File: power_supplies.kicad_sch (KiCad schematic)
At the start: 1 part, among them J3 12V supply

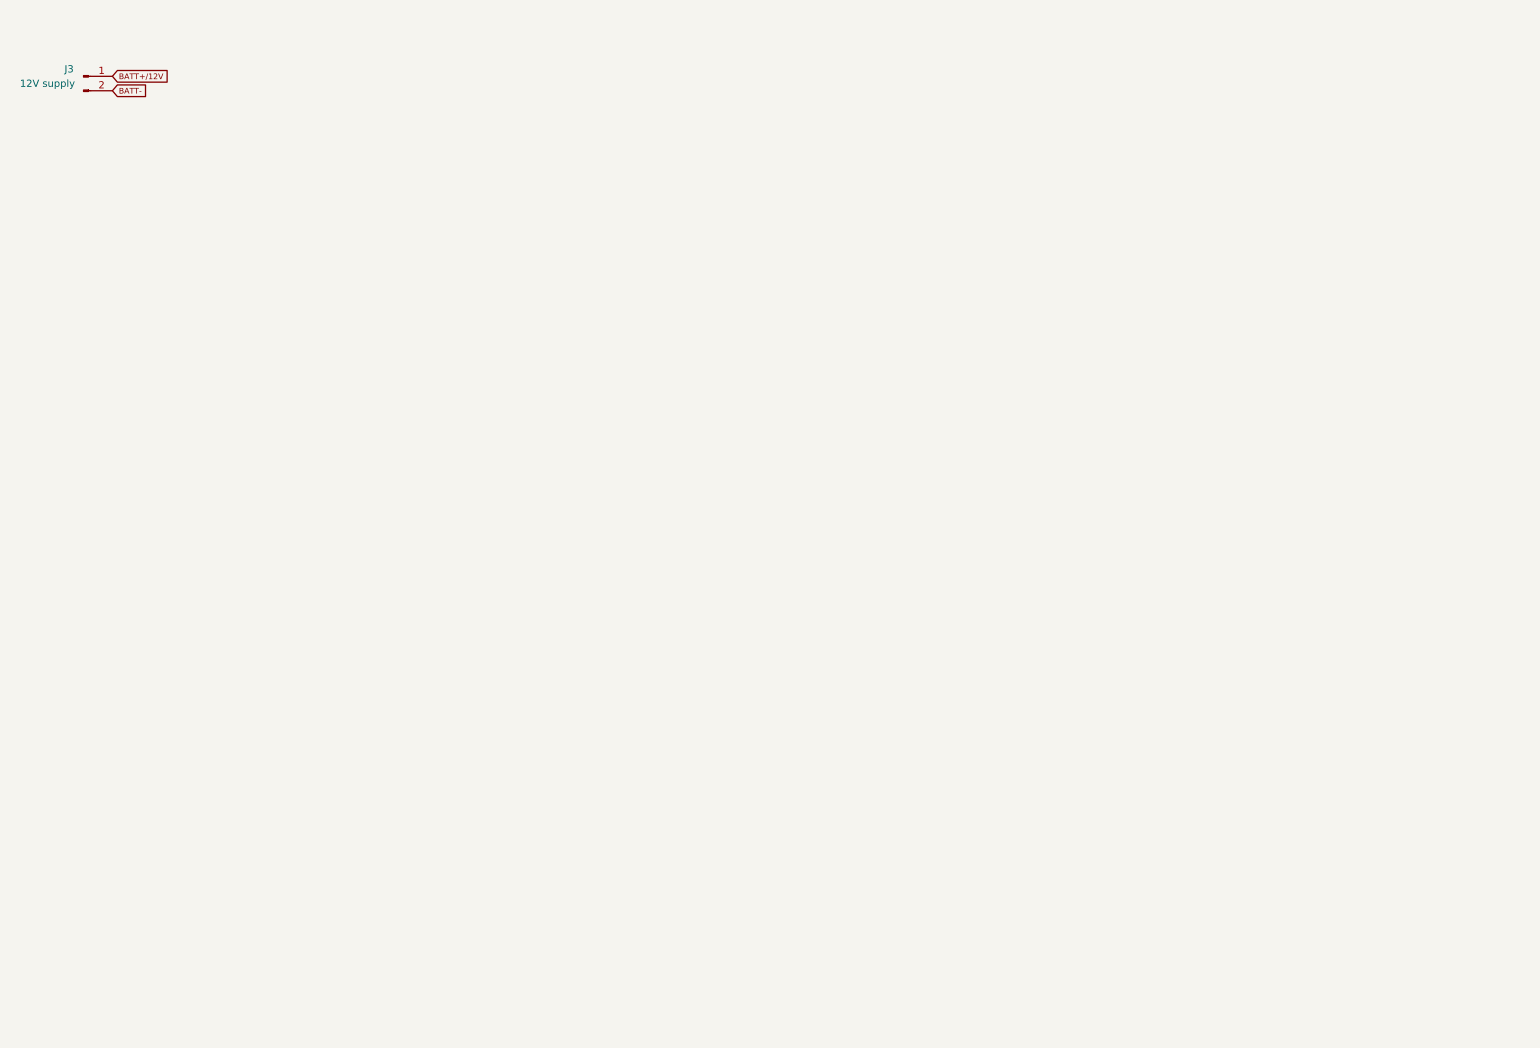
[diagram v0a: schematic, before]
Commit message: face to face switches design
with no MOVs and all other present
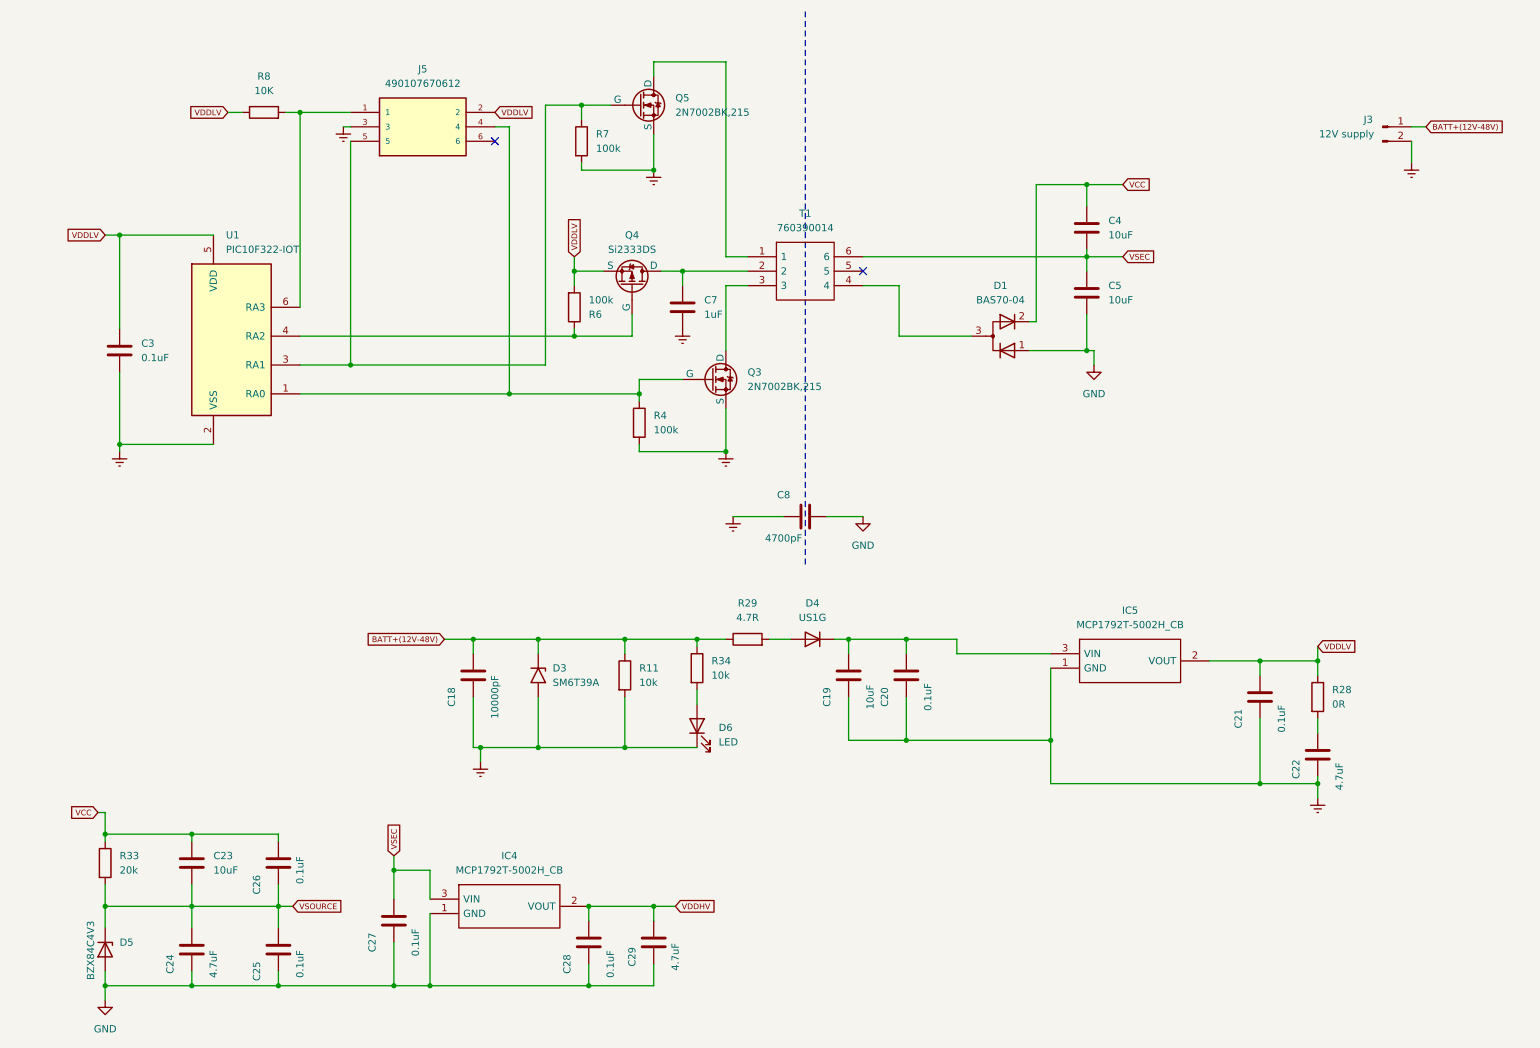
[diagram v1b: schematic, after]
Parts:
- added C18: 10000pF, Capacitor_SMD:C_0805_2012Metric, symbol Device:C
- added C19, C23: 10uF, Capacitor_SMD:C_0805_2012Metric, symbol Device:C
- added C20, C21, C25, C26, C27, C28, C3: 0.1uF, Capacitor_SMD:C_0805_2012Metric, symbol Device:C
- added C22: 4.7uF, Capacitor_SMD:C_0805_2012Metric, symbol Device:C
- added C24, C29: 4.7uF, Capacitor_SMD:C_1206_3216Metric, symbol Device:C
- added C4, C5: 10uF, Capacitor_SMD:C_1206_3216Metric, symbol Device:C
- added C7: 1uF, Capacitor_SMD:C_0805_2012Metric, symbol Device:C
- added C8: 4700pF, Capacitor_SMD:C_1812_4532Metric, symbol Device:C
- added D1: BAS70-04, Package_TO_SOT_SMD:SOT-23-3, symbol Device:D_Dual_Series_ACK_Parallel
- added D3: SM6T39A, Diode_SMD:D_SMB, symbol Diode:SM6T39A
- added D4: US1G, Diode_SMD:D_SMA, symbol Diode:US1G
- added D5: BZX84C4V3, Package_TO_SOT_SMD:SOT-23, symbol Device:D_Zener
- added D6: LED, LED_SMD:LED_0805_2012Metric, symbol Device:LED
- added IC4, IC5: MCP1792T-5002H_CB, MCP1792T-5002H_CB:SOT95P255X145-3N, symbol MCP1792T-5002H_CB:MCP1792T-5002H_CB
- added J5: 490107670612, 490107670612:WURTH_490107670612, symbol 490107670612:490107670612
- added Q3, Q5: 2N7002BK,215, Package_TO_SOT_SMD:SOT-23, symbol Simulation_SPICE:NMOS
- added Q4: Si2333DS, Package_TO_SOT_SMD:SOT-23-3, symbol Simulation_SPICE:PMOS
- added R11, R34: 10k, Resistor_SMD:R_0805_2012Metric, symbol Device:R
- added R28: 0R, Resistor_SMD:R_0805_2012Metric, symbol Device:R
- added R29: 4.7R, Resistor_SMD:R_0805_2012Metric, symbol Device:R
- added R33: 20k, Resistor_SMD:R_0805_2012Metric, symbol Device:R
- added R4, R6, R7: 100k, Resistor_SMD:R_0805_2012Metric, symbol Device:R
- added R8: 10K, Resistor_SMD:R_0805_2012Metric, symbol Device:R
- added T1: 760390014, push pull Transformer:760390015, symbol 760390014:760390014
- added U1: PIC10F322-IOT, Package_TO_SOT_SMD:SOT-23-6, symbol MCU_Microchip_PIC10:PIC10F322-IOT
- J3: footprint (none) -> TerminalBlock_Phoenix:TerminalBlock_Phoenix_MKDS-1,5-2_1x02_P5.00mm_Horizontal
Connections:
- net BATT+/12V renamed BATT+(12V-48V)
- net BATT+(12V-48V): now also C18.2, D3.1 (A1), R11.1, R29.1, R34.1
- net BATT- renamed Earth
- net Earth: now also C18.1, C19.1, C20.1, C21.1, C22.1, C3.2, C7.2, C8.1, D3.2 (A2), D6.1 (K), IC5.1 (GND), J5.3, Q3.2 (S), Q5.2 (S), R11.2, R4.2, R7.2, U1.2 (VSS)
- new net: J5.4, Q3.1 (G), R4.1, U1.1 (RA0)
- new net: J5.5, Q5.1 (G), R7.1, U1.3 (RA1)
- new net: Q4.1 (G), R6.1, U1.4 (RA2)
- new net: J5.1, R8.2, U1.6 (RA3)
- new net: D6.2 (A), R34.2
- new net: C19.2, C20.2, D4.1 (K), IC5.3 (VIN)
- new net: Q3.3 (D), T1.3
- new net: C7.1, Q4.3 (D), T1.2
- new net: Q5.3 (D), T1.1
- new net: D1.3 (A), T1.4
- new net: C22.2, R28.2
- new net: D4.2 (A), R29.2
- new net GND: C24.1, C25.1, C27.1, C28.1, C29.1, C5.2, C8.2, D1.1 (K), D5.2 (A), IC4.1 (GND)
- new net VCC: C23.1, C26.2, C4.1, D1.2 (K), R33.1
- new net VDDHV: C28.2, C29.2, IC4.2 (VOUT)
- new net VDDLV: C21.2, C3.1, IC5.2 (VOUT), J5.2, Q4.2 (S), R28.1, R6.2, R8.1, U1.5 (VDD)
- new net VSEC: C27.2, C4.2, C5.1, IC4.3 (VIN), T1.6
- new net VSOURCE: C23.2, C24.2, C25.2, C26.1, D5.1 (K), R33.2
- no-connect marks 0 -> 2
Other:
- moved on the sheet: J3

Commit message: updated the design
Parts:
- added TP3, TP8: TestPoint, TestPoint:TestPoint_Pad_D1.0mm, symbol Connector:TestPoint
- added TP9: 5001, 5001 tp:KEYSTONE_5001, symbol 5001:5001
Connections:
- net GND: now also TP9.TP
- net VCC: now also TP8.1
- net VSEC: now also TP3.1
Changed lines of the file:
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@@
   (junction (at 129.54 170.18) (diameter 0) (color 0 0 0 0)
   )
+  (junction (at 210.82 55.88) (diameter 0) (color 0 0 0 0)
+  )
   (junction (at 134.62 58.42) (diameter 0) (color 0 0 0 0)
   )
   (junction (at 115.57 58.42) (diameter 0) (color 0 0 0 0)
+  )
+  (junction (at 207.01 72.39) (diameter 0) (color 0 0 0 0)
   )
   (junction (at 99.06 142.24) (diameter 0) (color 0 0 0 0)
@@
   (no_connect (at 101.6 35.56))
   (no_connect (at 166.37 58.42))
-  (wire (pts (xy 205.74 55.88) (xy 212.09 55.88))
-    (stroke (width 0) (type default))
-  )
   (wire (pts (xy 116.84 39.37) (xy 116.84 40.64))
     (stroke (width 0) (type default))
@@
     (stroke (width 0) (type default))
   )
+  (wire (pts (xy 210.82 53.34) (xy 210.82 55.88))
+    (stroke (width 0) (type default))
+  )
   (wire (pts (xy 104.14 33.02) (xy 104.14 80.01))
     (stroke (width 0) (type default))
@@
     (stroke (width 0) (type default))
   )
+  (wire (pts (xy 205.74 33.02) (xy 205.74 43.18))
+    (stroke (width 0) (type default))
+  )
   (wire (pts (xy 33.02 153.67) (xy 33.02 157.48))
     (stroke (width 0) (type default))
@@
     (stroke (width 0) (type default))
   )
+  (wire (pts (xy 223.52 72.39) (xy 207.01 72.39))
+    (stroke (width 0) (type default))
+  )
   (wire (pts (xy 67.31 80.01) (xy 104.14 80.01))
     (stroke (width 0) (type default))
@@
     (stroke (width 0) (type default))
   )
+  (wire (pts (xy 223.52 53.34) (xy 210.82 53.34))
+    (stroke (width 0) (type default))
+  )
   (wire (pts (xy 173.99 123.19) (xy 173.99 125.73))
     (stroke (width 0) (type default))
@@
     (stroke (width 0) (type default))
   )
+  (wire (pts (xy 210.82 55.88) (xy 212.09 55.88))
+    (stroke (width 0) (type default))
+  )
   (wire (pts (xy 110.49 29.21) (xy 110.49 74.93))
     (stroke (width 0) (type default))
@@
   )
   (wire (pts (xy 124.46 123.19) (xy 124.46 125.73))
+    (stroke (width 0) (type default))
+  )
+  (wire (pts (xy 210.82 55.88) (xy 205.74 55.88))
     (stroke (width 0) (type default))
   )
@@
     )
   )
+  (symbol (lib_id "Connector:TestPoint") (at 205.74 33.02 0) (unit 1)
+    (in_bom yes) (on_board yes) (dnp no) (fields_autoplaced)
+    (property "Reference" "TP8" (at 208.28 28.448 0)
+      (effects (font (size 1.27 1.27)) (justify left))
+    )
+    (property "Value" "TestPoint" (at 208.28 30.988 0)
+      (effects (font (size 1.27 1.27)) (justify left))
+    )
+    (property "Footprint" "TestPoint:TestPoint_Pad_D1.0mm" (at 210.82 33.02 0)
+      (effects (font (size 1.27 1.27)) hide)
+    )
+    (property "Datasheet" "~" (at 210.82 33.02 0)
+      (effects (font (size 1.27 1.27)) hide)
+    )
+    (pin "1")
+    (instances
+      (project "SiC based Battery Disconnect"
+        (path "/525387b1-1528-4728-a616-6f57d2a34d69/925d75c4-de6e-4540-9e02-6341c2b379d1"
+          (reference "TP8") (unit 1)
+        )
+      )
+    )
+  )
   (symbol (lib_name "NMOS_1") (lib_id "Simulation_SPICE:NMOS") (at 139.7 77.47 0) (unit 1)
     (in_bom yes) (on_board yes) (dnp no) (fields_autoplaced)
@@
     )
   )
+  (symbol (lib_id "Connector:TestPoint") (at 223.52 53.34 0) (unit 1)
+    (in_bom yes) (on_board yes) (dnp no) (fields_autoplaced)
+    (property "Reference" "TP3" (at 226.06 48.768 0)
+      (effects (font (size 1.27 1.27)) (justify left))
+    )
+    (property "Value" "TestPoint" (at 226.06 51.308 0)
+      (effects (font (size 1.27 1.27)) (justify left))
+    )
+    (property "Footprint" "TestPoint:TestPoint_Pad_D1.0mm" (at 228.6 53.34 0)
+      (effects (font (size 1.27 1.27)) hide)
+    )
+    (property "Datasheet" "~" (at 228.6 53.34 0)
+      (effects (font (size 1.27 1.27)) hide)
+    )
+    (pin "1")
+    (instances
+      (project "SiC based Battery Disconnect"
+        (path "/525387b1-1528-4728-a616-6f57d2a34d69/925d75c4-de6e-4540-9e02-6341c2b379d1"
+          (reference "TP3") (unit 1)
+        )
+      )
+    )
+  )
   (symbol (lib_name "NMOS_1") (lib_id "Simulation_SPICE:NMOS") (at 127 29.21 0) (unit 1)
     (in_bom yes) (on_board yes) (dnp no) (fields_autoplaced)
@@
         )
       )
+    )
+  )
+  (symbol (lib_id "5001:5001") (at 223.52 67.31 90) (unit 1)
+    (in_bom yes) (on_board yes) (dnp no) (fields_autoplaced)
+    (property "Reference" "TP9" (at 226.06 66.04 90)
+      (effects (font (size 1.27 1.27)) (justify right))
+    )
+    (property "Value" "5001" (at 226.06 68.58 90)
+      (effects (font (size 1.27 1.27)) (justify right))
+    )
+    (property "Footprint" "5001 tp:KEYSTONE_5001" (at 223.52 67.31 0)
+      (effects (font (size 1.27 1.27)) (justify bottom) hide)
+    )
+    (property "Datasheet" "" (at 223.52 67.31 0)
+      (effects (font (size 1.27 1.27)) hide)
+    )
+    (property "MF" "Keystone Electronics Corp." (at 223.52 67.31 0)
+      (effects (font (size 1.27 1.27)) (justify bottom) hide)
+    )
+    (property "MAXIMUM_PACKAGE_HEIGHT" "4.57 mm" (at 223.52 67.31 0)
+      (effects (font (size 1.27 1.27)) (justify bottom) hide)
+    )
+    (property "Package" "None" (at 223.52 67.31 0)
+      (effects (font (size 1.27 1.27)) (justify bottom) hide)
+    )
+    (property "Price" "None" (at 223.52 67.31 0)
+      (effects (font (size 1.27 1.27)) (justify bottom) hide)
+    )
+    (property "Check_prices" "https://www.snapeda.com/parts/5001/Keystone+Electronics/view-part/?ref=eda" (at 223.52 67.31 0)
+      (effects (font (size 1.27 1.27)) (justify bottom) hide)
+    )
+    (property "STANDARD" "Manufacturer Recommendations" (at 223.52 67.31 0)
+      (effects (font (size 1.27 1.27)) (justify bottom) hide)
+    )
+    (property "PARTREV" "H" (at 223.52 67.31 0)
+      (effects (font (size 1.27 1.27)) (justify bottom) hide)
+    )
+    (property "SnapEDA_Link" "https://www.snapeda.com/parts/5001/Keystone+Electronics/view-part/?ref=snap" (at 223.52 67.31 0)
+      (effects (font (size 1.27 1.27)) (justify bottom) hide)
+    )
+    (property "MP" "5001" (at 223.52 67.31 0)
+      (effects (font (size 1.27 1.27)) (justify bottom) hide)
+    )
+    (property "Description" "\nBlack PC Test Point, Miniature Phosphor Bronze Silver Plating 0.040 (1.02mm) Hole Diameter Mounting Type\n" (at 223.52 67.31 0)
+      (effects (font (size 1.27 1.27)) (justify bottom) hide)
+    )
+    (property "MANUFACTURER" "Keystone" (at 223.52 67.31 0)
+      (effects (font (size 1.27 1.27)) (justify bottom) hide)
+    )
+    (property "Availability" "In Stock" (at 223.52 67.31 0)
+      (effects (font (size 1.27 1.27)) (justify bottom) hide)
+    )
+    (property "SNAPEDA_PN" "5000" (at 223.52 67.31 0)
+      (effects (font (size 1.27 1.27)) (justify bottom) hide)
+    )
+    (pin "TP")
+    (instances
+      (project "SiC based Battery Disconnect"
+        (path "/525387b1-1528-4728-a616-6f57d2a34d69/a4af0f90-9694-45a8-86a1-2f9082dd6b02"
+          (reference "TP9") (unit 1)
+        )
+        (path "/525387b1-1528-4728-a616-6f57d2a34d69/925d75c4-de6e-4540-9e02-6341c2b379d1"
+          (reference "TP5") (unit 1)
+        )
+      )

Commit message: design update
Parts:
- added C17: 0.1uF, Capacitor_SMD:C_0805_2012Metric, symbol Device:C
- D5: value BZX84C4V3 -> BZX84C6V8
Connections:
- net Earth: now also C17.1
- net VDDLV: now also C17.2
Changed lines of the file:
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@@
   (junction (at 118.11 170.18) (diameter 0) (color 0 0 0 0)
+  )
+  (junction (at 109.22 13.97) (diameter 0) (color 0 0 0 0)
   )
   (junction (at 236.22 148.59) (diameter 0) (color 0 0 0 0)
@@
     (stroke (width 0) (type default))
   )
+  (wire (pts (xy 104.14 13.97) (xy 104.14 30.48))
+    (stroke (width 0) (type default))
+  )
   (wire (pts (xy 33.02 158.75) (xy 33.02 157.48))
     (stroke (width 0) (type default))
@@
     (stroke (width 0) (type default))
   )
+  (wire (pts (xy 114.3 13.97) (xy 109.22 13.97))
+    (stroke (width 0) (type default))
+  )
   (wire (pts (xy 124.46 142.24) (xy 137.16 142.24))
     (stroke (width 0) (type default))
@@
     (stroke (width 0) (type default))
   )
+  (wire (pts (xy 104.14 13.97) (xy 109.22 13.97))
+    (stroke (width 0) (type default))
+  )
   (wire (pts (xy 67.31 74.93) (xy 76.2 74.93))
     (stroke (width 0) (type default))
@@
     (stroke (width 0) (type default))
   )
+  (wire (pts (xy 104.14 30.48) (xy 101.6 30.48))
+    (stroke (width 0) (type default))
+  )
   (wire (pts (xy 92.71 123.19) (xy 97.79 123.19))
     (stroke (width 0) (type default))
@@
   )
   (wire (pts (xy 143.51 101.6) (xy 152.4 101.6))
+    (stroke (width 0) (type default))
+  )
+  (wire (pts (xy 109.22 13.97) (xy 109.22 15.24))
     (stroke (width 0) (type default))
   )
@@
     )
   )
-  (global_label "VDDLV" (shape input) (at 101.6 30.48 0) (fields_autoplaced)
+  (global_label "VDDLV" (shape input) (at 114.3 13.97 0) (fields_autoplaced)
     (effects (font (size 1 1)) (justify left))
-    (property "Intersheetrefs" "${INTERSHEET_REFS}" (at 108.474 30.48 0)
+    (property "Intersheetrefs" "${INTERSHEET_REFS}" (at 121.174 13.97 0)
       (effects (font (size 1.27 1.27)) (justify left) hide)
     )
@@
     )
   )
+  (symbol (lib_id "Device:C") (at 109.22 19.05 180) (unit 1)
+    (in_bom yes) (on_board yes) (dnp no)
+    (property "Reference" "C17" (at 106.68 21.59 90)
+      (effects (font (size 1.27 1.27)))
+    )
+    (property "Value" "0.1uF" (at 113.03 22.86 90)
+      (effects (font (size 1.27 1.27)))
+    )
+    (property "Footprint" "Capacitor_SMD:C_0805_2012Metric" (at 108.2548 15.24 0)
+      (effects (font (size 1.27 1.27)) hide)
+    )
+    (property "Datasheet" "~" (at 109.22 19.05 0)
+      (effects (font (size 1.27 1.27)) hide)
+    )
+    (pin "1")
+    (pin "2")
+    (instances
+      (project "SiC based Battery Disconnect"
+        (path "/525387b1-1528-4728-a616-6f57d2a34d69/925d75c4-de6e-4540-9e02-6341c2b379d1"
+          (reference "C17") (unit 1)
+        )
+      )
+    )
+  )
   (symbol (lib_id "Device:C") (at 48.26 162.56 0) (unit 1)
     (in_bom yes) (on_board yes) (dnp no) (fields_autoplaced)
@@
         (path "/525387b1-1528-4728-a616-6f57d2a34d69/925d75c4-de6e-4540-9e02-6341c2b379d1"
           (reference "C26") (unit 1)
+        )
+      )
+    )
+  )
+  (symbol (lib_id "power:Earth") (at 109.22 22.86 0) (unit 1)
+    (in_bom yes) (on_board yes) (dnp no) (fields_autoplaced)
+    (property "Reference" "#PWR09" (at 109.22 29.21 0)
+      (effects (font (size 1.27 1.27)) hide)
+    )
+    (property "Value" "Earth" (at 109.22 26.67 0)
+      (effects (font (size 1.27 1.27)) hide)
+    )
+    (property "Footprint" "" (at 109.22 22.86 0)
+      (effects (font (size 1.27 1.27)) hide)
+    )
+    (property "Datasheet" "~" (at 109.22 22.86 0)
+      (effects (font (size 1.27 1.27)) hide)
+    )
+    (pin "1")
+    (instances
+      (project "SiC based Battery Disconnect"
+        (path "/525387b1-1528-4728-a616-6f57d2a34d69/925d75c4-de6e-4540-9e02-6341c2b379d1"
+          (reference "#PWR09") (unit 1)
         )
       )
@@
       (effects (font (size 1.27 1.27)) (justify left))
     )
-    (property "Value" "BZX84C4V3" (at 30.48 172.72 0)
-      (effects (font (size 1.27 1.27)) (justify left))
-    )
+    (property "Value" "BZX84C6V8" (at 30.48 172.72 0)
+      (effects (font (size 1.27 1.27)) (justify left))
+    )
